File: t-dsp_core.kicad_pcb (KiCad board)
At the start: 4 copper layers, 100 x 61 mm, 165 parts, among them IC1 Logic Level Shifter - 74HCT2G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, J1 J_PWR, J10 J_DMX, J11 J_LED, J12 J_ETH, J13 u.FL DNP (IDC767 ext-antenna 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, J2 J_TDM, J3 J_T, J4 J_USB, J5 J_MIDI, J7 J_SAI2, J8 J_S3, Q1 AO3401A, T108 Tab, T109 Tab, T110 Tab, T111 Tab, U1 Teensy 4.1 - DEVKIT, U11 Dual Buffer - SN74LVC2G125DCTR, U13 ESP32-S3-WROOM-1-N16R8, U15 LT3045EMSE#TRPBF, U19 SN74LVC257APWR, U20 SN74LVC2G125DCTR, U21 SN74LVC244APWR, U22 IDC777-1, U23 SN74LVC138APWR, U24 AP63203WU, U4 Optoisolators - H11L1SM - 6-S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, U5 SN74LVC541APWR, U6 SN74LVC2G125DCTR, U7 SN74LVC2G125DCTR, U9 Dual Buffer - 74HCT2G17GW,125, Y1 24.576MHz

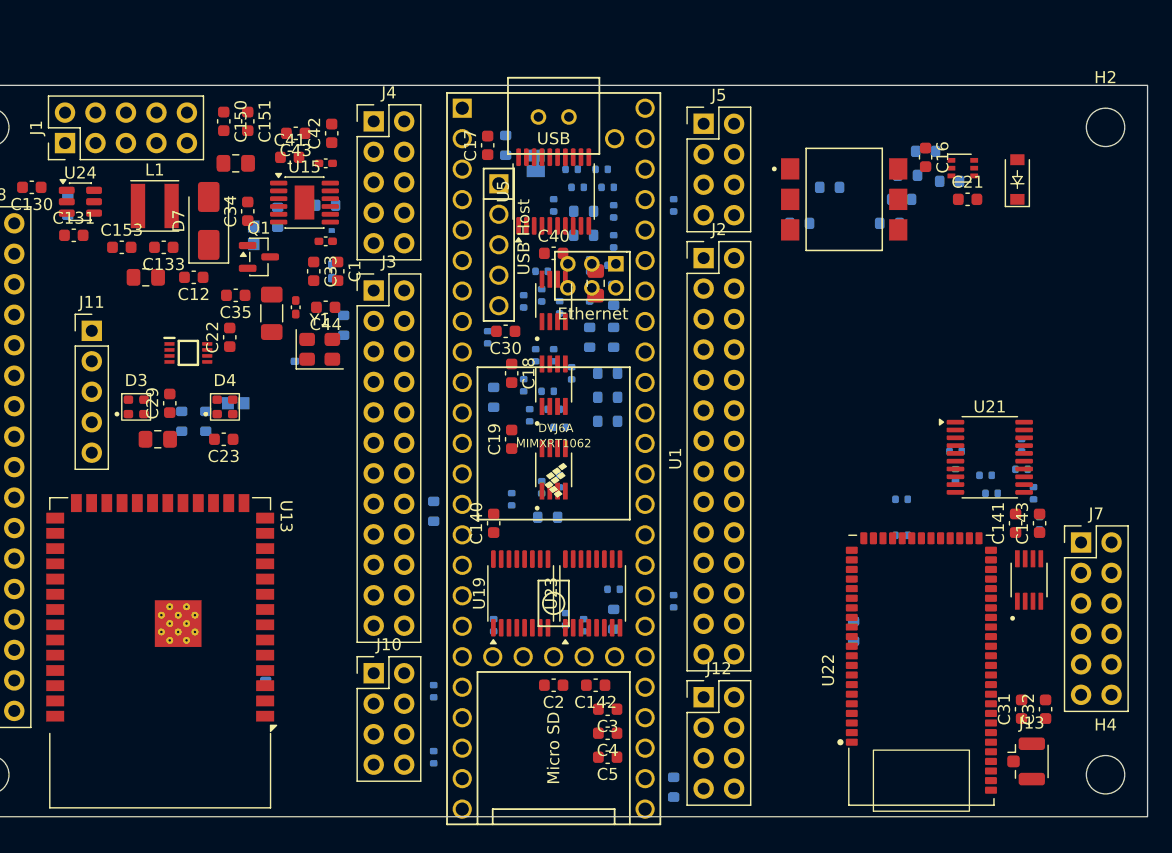
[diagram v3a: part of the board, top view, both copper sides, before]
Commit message: Spin 2 stage 11a (board + docs): four GPIO columns, LED block to the right slot, J10 removed
- Columns: A J8 (S3 IO); B J2 + J7 (TDM, SAI2) left of the Teensy; C J4 + J3 + J12 (USB, Teensy GPIO, Ethernet) right of it; D J5 + J11 (MIDI, LED) on the right edge. J1 power stays on the top edge.
- IC1/D3/D4 beside J11; U21/U20 under the Teensy beside J7; U11/U6/U7 shifted below the Teensy41 Ethernet pads.
- Passives re-placed (123, median 2.2 mm, mean 3.1 mm). MST ratsnest 4415 -> 3900 mm. DRC with parity: known cosmetic residue only.
- Change map 11.10 added, section 13 regenerated from the netlist.

Co-Authored-By: Claude Fable 5.1 <noreply@anthropic.com>
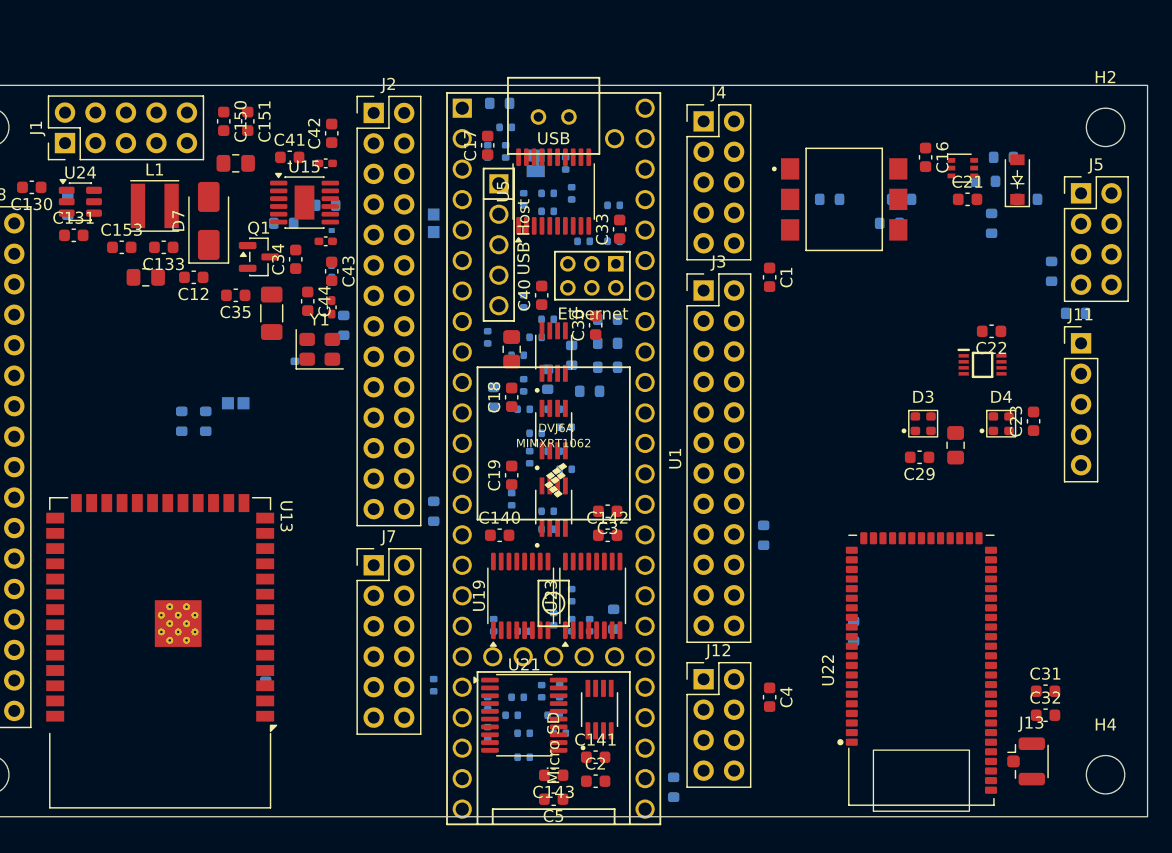
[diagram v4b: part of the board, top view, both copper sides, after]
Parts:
- removed J10: J_DMX, Connector_PinHeader_2.54mm:PinHeader_2x04_P2.54mm_Vertical
- moved J11 82.5 mm to (194.5, 160.5)
- moved C23 67.5 mm to (190.5, 167.0), turned to 90 degrees
- moved C28 66.5 mm to (184.0, 169.0), turned to -90 degrees
- moved IC1 66.2 mm to (186.2, 162.3)
- moved D3 65.6 mm to (181.3, 167.2)
- moved D4 64.7 mm to (187.8, 167.2)
- moved C22 63.5 mm to (187.0, 159.5), turned to 180 degrees
- moved C29 62.7 mm to (181.0, 170.0), turned to 180 degrees
- moved J7 59.0 mm to (135.5, 179.0)
- moved R97 49.2 mm to (140.5, 189.0), turned to 90 degrees
- moved R94 46.4 mm to (148.0, 193.0), turned to 180 degrees
- moved R101 46.2 mm to (147.5, 190.0), turned to 180 degrees
- moved C143 45.6 mm to (150.5, 196.5), turned to 180 degrees
- moved R92 45.0 mm to (150.5, 191.5), turned to 180 degrees
- moved R95 44.5 mm to (145.0, 193.0)
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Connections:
- J3 pad 17: GND -> T38
- J3 pad 18: GND -> T39
- J3 pad 19: GND -> T40
- J8 pad 10: S3_IO47_SCL -> S3_USB_DP
- J8 pad 11: S3_IO18 -> GND
- J8 pad 12: S3_IO9 -> 5V
- J8 pad 13: S3_IO10 -> S3_IO9
- J8 pad 14: S3_IO11 -> S3_IO10
- J8 pad 15: GND -> S3_IO11
- J8 pad 17: S3_IO2 -> S3_IO21_SDA
- J8 pad 18: S3_IO42 -> S3_IO47_SCL
- J8 pad 19: S3_IO8 -> S3_IO48
- J8 pad 20: T40 -> S3_IO45
- J8 pad 21: T39 -> GND
- J8 pad 22: T38 -> GND
- J8 pad 23: S3_IO15 -> S3_IO0_BOOT
- J8 pad 25: GND -> S3_IO39
- J8 pad 26: GND -> S3_IO42
- J8 pad 27: S3_IO45 -> GND
- J8 pad 28: S3_IO39 -> GND
- J8 pad 29: GND -> /S3_IO44_RXD0
- J8 pad 3: /S3_IO43_TXD0 -> S3_EN
- J8 pad 30: GND -> /S3_IO43_TXD0
- J8 pad 31: S3_USB_DN -> S3_IO2
- J8 pad 32: S3_USB_DP -> S3_IO1
- J8 pad 34: 5V -> GND
- J8 pad 4: /S3_IO44_RXD0 -> S3_IO5
- J8 pad 5: S3_EN -> S3_IO15
- J8 pad 6: S3_IO0_BOOT -> S3_IO18
- J8 pad 7: GND -> S3_IO8
- J8 pad 9: S3_IO21_SDA -> S3_USB_DN
- U13 pad 25: DMX_DE -> S3_IO48
- U13 pad 39: DMX_RX -> S3_IO1
- U13 pad 5: DMX_TX -> S3_IO5

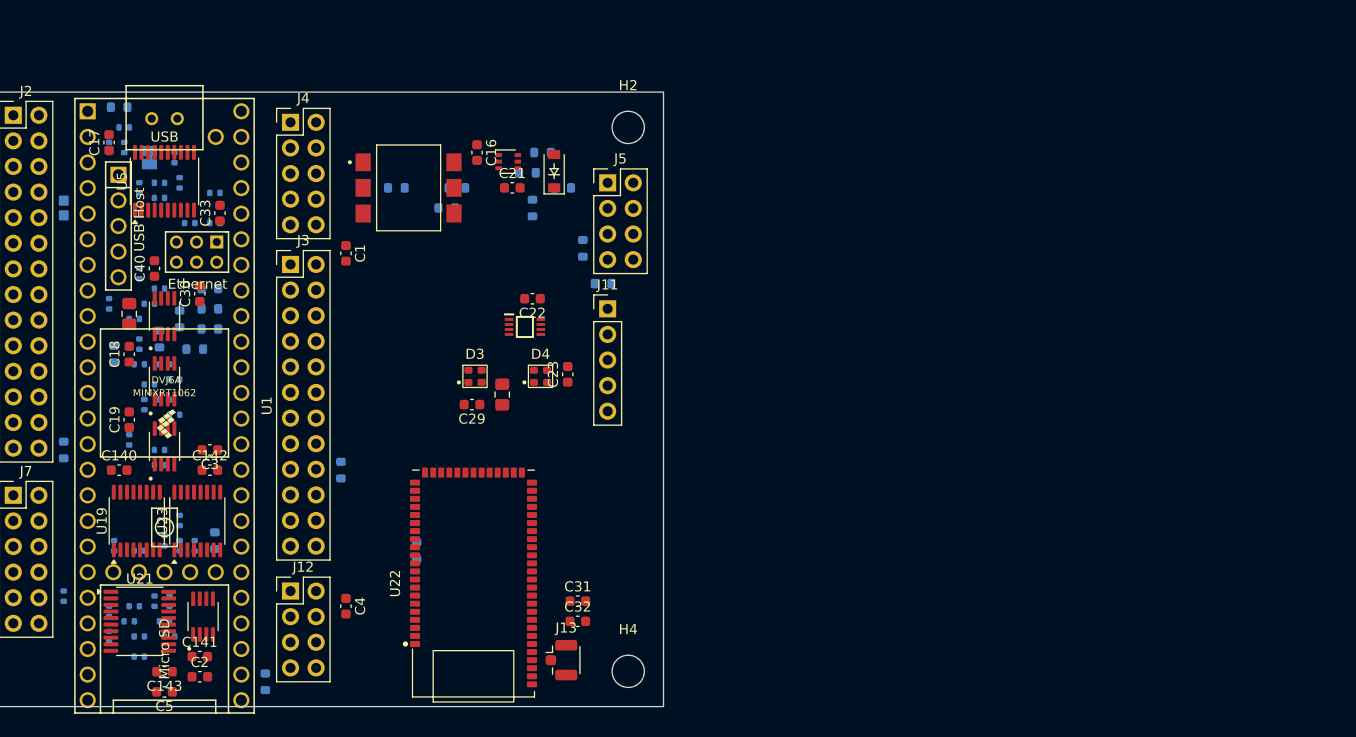
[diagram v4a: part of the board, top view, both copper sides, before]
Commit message: User edits saved from eeschema and the PCB Editor
Co-Authored-By: Claude Fable 5.1 <noreply@anthropic.com>
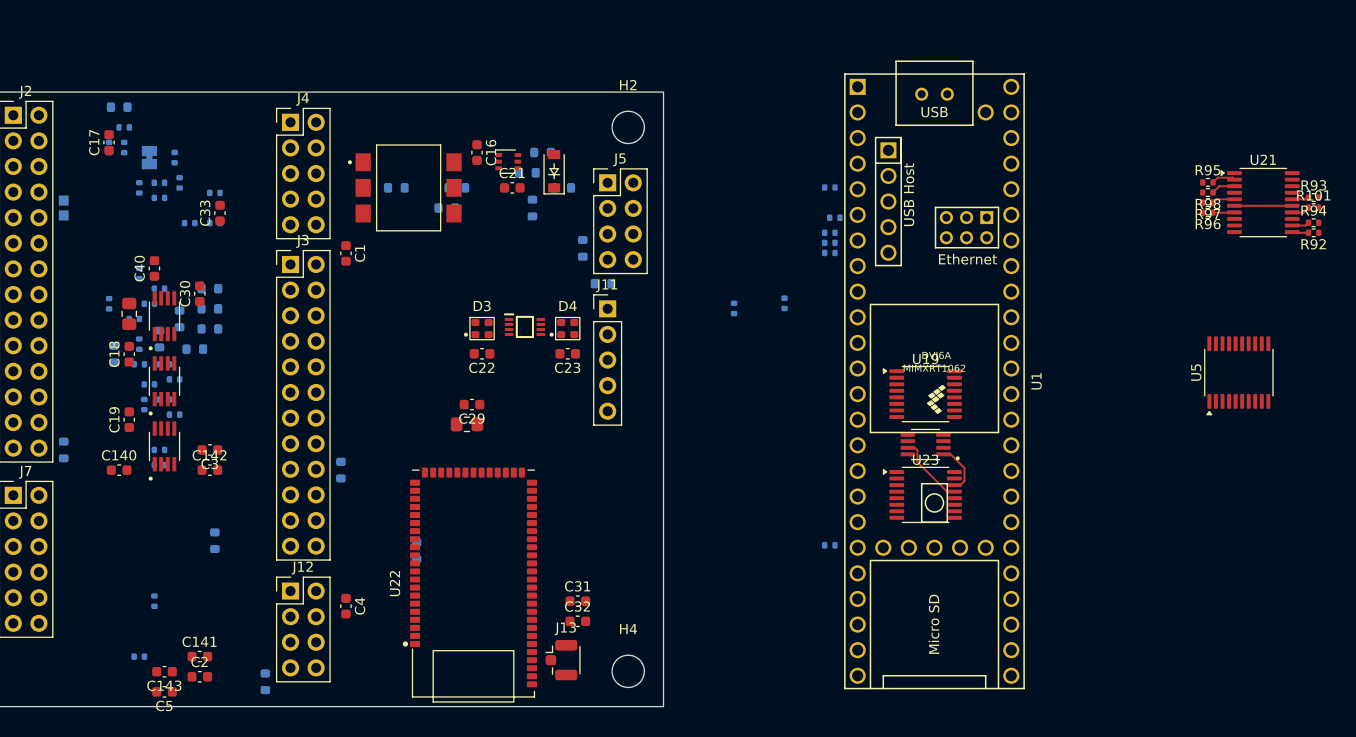
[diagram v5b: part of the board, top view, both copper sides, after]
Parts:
- R101, R92, R93, R94, R95, R96, R97, R98: moved to F.Cu
- moved R94 123.5 mm to (264.5, 152.0), turned to 0 degrees
- moved R101 123.5 mm to (264.5, 150.5), turned to 0 degrees
- moved R93 121.6 mm to (264.5, 149.5), turned to 0 degrees
- moved R92 120.3 mm to (264.5, 153.0)
- moved R97 120.0 mm to (254.0, 150.0), turned to 180 degrees
- moved U21 118.9 mm to (259.5, 150.0)
- moved R95 117.9 mm to (254.0, 148.0), turned to 0 degrees
- moved R96 116.0 mm to (254.0, 151.0), turned to 180 degrees
- moved R98 115.1 mm to (254.0, 149.0), turned to 180 degrees
- moved U5 108.3 mm to (257.1, 166.9)
- moved U19 79.3 mm to (226.0, 169.0), turned to 0 degrees
- moved R90 77.3 mm to (216.5, 148.5), turned to 0 degrees
- moved R89 76.5 mm to (217.0, 151.5)
- moved U1 76.4 mm to (226.9, 198.2)
- moved U20 73.7 mm to (226.0, 174.0), turned to 180 degrees
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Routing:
- net SAI2_nOE_OUT: track 0.00 -> 7.12 mm
- net SAI2_MCLK: track 0.00 -> 5.73 mm
- net SAI2_nOE_HDR: track 0.00 -> 5.08 mm
- net AUX_I2S_BCK: track 0.00 -> 2.41 mm
- net Net-(U21-O3b): track 0.00 -> 2.39 mm
- net Net-(U21-O2b): track 0.00 -> 2.26 mm
- net Net-(U21-O1b): track 0.00 -> 2.14 mm
- net Net-(U21-O2a): track 0.00 -> 1.83 mm
- net Net-(U21-O3a): track 0.00 -> 1.73 mm
- net Net-(U21-O1a): track 0.00 -> 1.70 mm
- net SAI2_BCLK: track 0.00 -> 1.65 mm

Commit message: Spin 2 stage 11b: all 0402 resistors to 0603 (footprints swapped in place, no re-placement)
- 33 x 33 R (C23140), 10 x 0 R jumpers (C21189), 3 x 10 k (C25804) now Resistor_SMD:R_0603_1608Metric in schematic and board; positions and rotations unchanged, the 30 routed track segments kept.
- Known result of swapping without re-placing: 26 resistor courtyard overlaps, 18 pad-to-pad clearance errors (0.05-0.10 mm) and one existing track (Net-(U21-O3b)) now touching R95 pad 2. These need manual nudging.
- Capacitors C45, C46, C129 stay 0402.

Co-Authored-By: Claude Fable 5.1 <noreply@anthropic.com>
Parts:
- R100, R101, R3, R4, R40, R41, R42, R43, R44, R45, R46, R47, R5, R52, R55, R56, R6, R7, R75, R76, R77, R78, R79, R80, R81, R82, R83, R84, R85, R86, R87, R88, R89, R9, R90, R91, R92, R93, R94, R95, R96, R97, R98, R99: footprint Resistor_SMD:R_0402_1005Metric -> Resistor_SMD:R_0603_1608Metric
- R59, R60: footprint Capacitor_SMD:C_0402_1005Metric_Pad0.74x0.62mm_HandSolder -> Resistor_SMD:R_0603_1608Metric

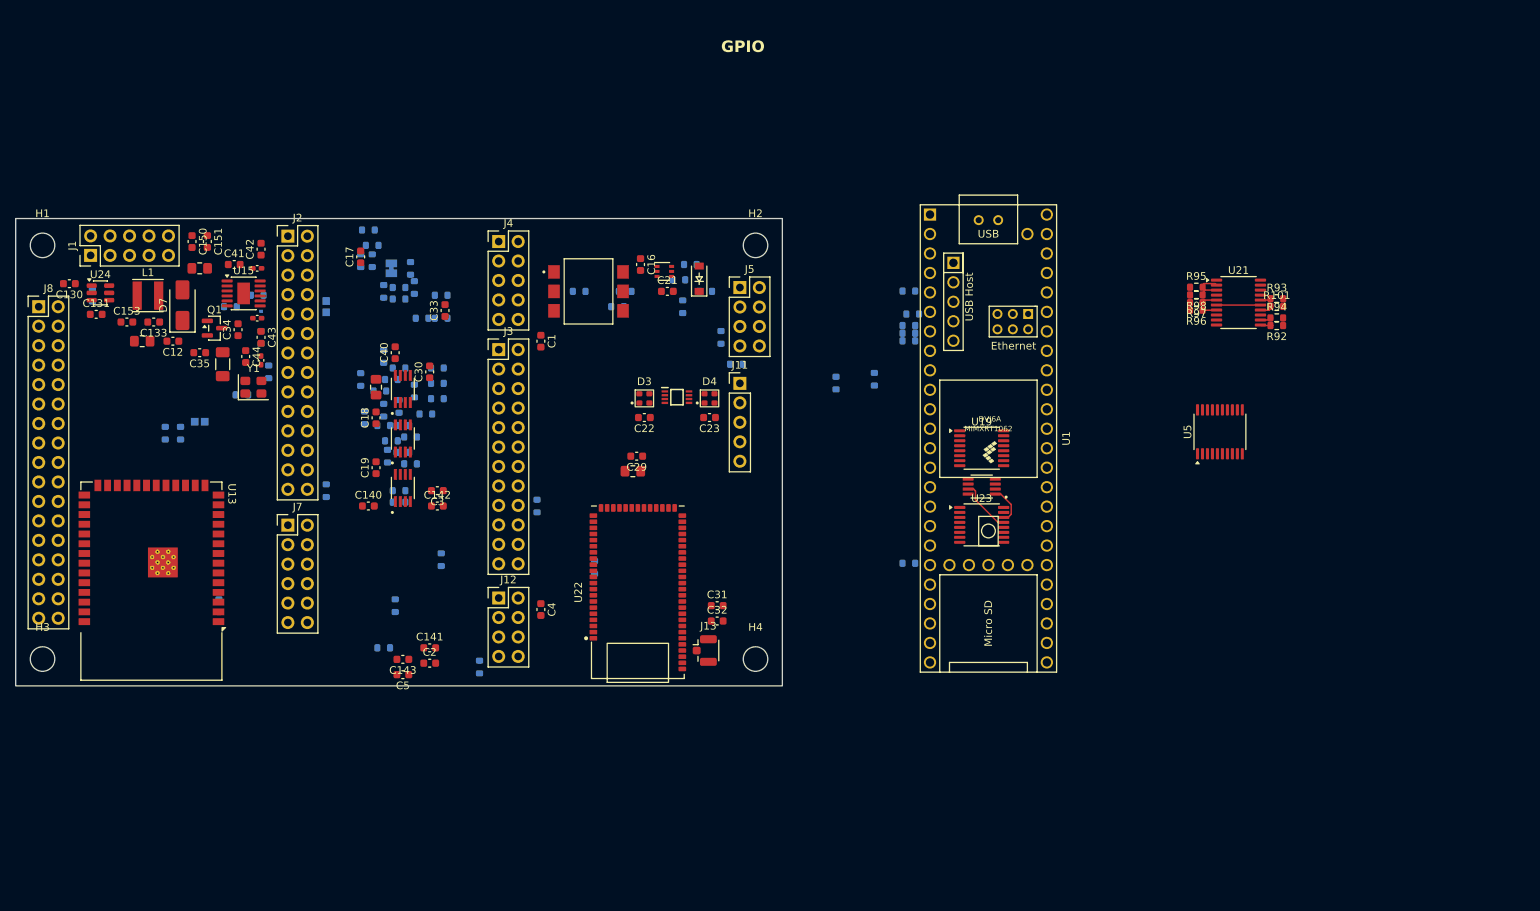
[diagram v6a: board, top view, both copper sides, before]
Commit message: User routing and staging saved from the PCB Editor (U5 fan-out group)
Co-Authored-By: Claude Fable 5.1 <noreply@anthropic.com>
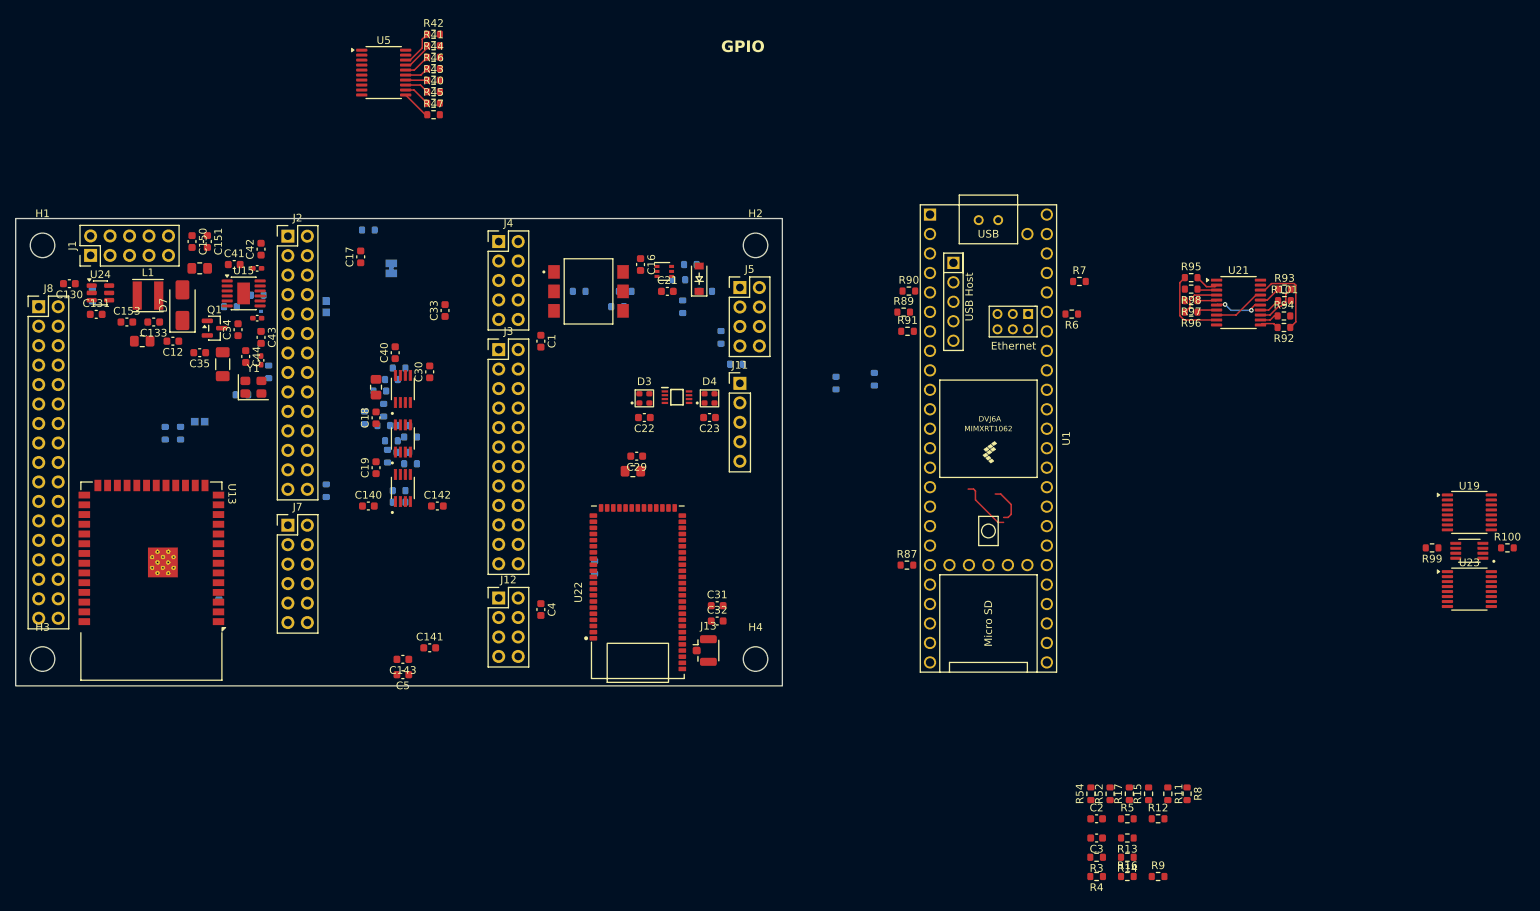
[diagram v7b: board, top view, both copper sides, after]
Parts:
- R100, R11, R12, R13, R14, R15, R16, R17, R3, R4, R40, R41, R42, R43, R44, R45, R46, R47, R5, R52, R54, R6, R7, R8, R87, R89, R9, R90, R91, R99: moved to F.Cu
- moved R9 120.5 mm to (249.0, 224.9), turned to 0 degrees
- moved U5 118.7 mm to (148.0, 120.0), turned to 0 degrees
- moved R4 115.1 mm to (241.0, 224.9), turned to 180 degrees
- moved R3 114.4 mm to (241.0, 222.4), turned to 180 degrees
- moved R12 110.9 mm to (249.0, 217.3), turned to 0 degrees
- moved R16 109.6 mm to (245.0, 224.9), turned to 0 degrees
- moved R15 109.2 mm to (247.8, 214.1)
- moved R14 108.1 mm to (245.0, 222.4), turned to 180 degrees
- moved R17 107.8 mm to (245.3, 214.1)
- moved R13 107.8 mm to (245.0, 219.8), turned to 180 degrees
- moved R11 99.6 mm to (250.3, 214.1)
- moved R5 99.5 mm to (245.0, 217.3), turned to 0 degrees
- moved C3 97.2 mm to (241.0, 219.8)
- moved R52 96.4 mm to (242.8, 214.1)
- moved R8 92.7 mm to (252.8, 214.1)
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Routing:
- net Net-(U21-O0a): track 0.00 -> 10.9 mm
- net Net-(U21-O0b): track 0.00 -> 10.3 mm
- net SAI2_OUT: track 0.00 -> 6.80 mm
- net SAI2_LRCLK: track 0.00 -> 5.92 mm
- net AUX_I2S_LRCK: track 0.00 -> 5.63 mm
- net /TDM1_LRCK_B: track 0.00 -> 4.88 mm
- net /TDM1_MCLK_B: track 0.00 -> 4.03 mm
- net /TDM2_DOUT_B: track 0.00 -> 3.88 mm
- net /TDM2_BCLK_B: track 0.00 -> 3.53 mm
- net /TDM1_BCLK_B: track 0.00 -> 3.51 mm
- net /TDM2_MCLK_B: track 0.00 -> 3.17 mm
- net /TDM1_DOUT_B: track 0.00 -> 3.15 mm
- net /TDM2_LRCK_B: track 0.00 -> 2.82 mm
- net Net-(U21-O1a): track 1.70 -> 2.90 mm
- net Net-(U21-O2a): track 1.83 -> 2.81 mm
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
